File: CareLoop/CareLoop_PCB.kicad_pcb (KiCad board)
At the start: 2 copper layers, 67 parts, among them J1 Conn_Coaxial_Small, J1_Battery1 Conn_01x02_Pin, J1_DEBUG1 Conn_01x04_Pin, J2 USB_B_Micro, U1 MCP1700x-180xxMB, U2 MAX30102, U3 MPU-6050, U4 MCP1700x-330xxMB, U5 TP4056-42-ESOP8, U6 nRF52840-QFXX, U7 PCA9306, Y1 32MHz, Y2 32.768kHz

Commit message: update
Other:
- copper layers 2 -> 6
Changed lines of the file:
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@@
 	(layers
 		(0 "F.Cu" signal)
+		(4 "In1.Cu" signal)
+		(6 "In2.Cu" signal)
+		(8 "In3.Cu" signal)
+		(10 "In4.Cu" signal)
 		(2 "B.Cu" signal)
 		(9 "F.Adhes" user "F.Adhesive")
@@
 			)
 			(layer "dielectric 1"
-				(type "core")
-				(thickness 0.8)
+				(type "prepreg")
+				(thickness 0.1)
 				(material "FR4")
 				(epsilon_r 4.3)
 				(loss_tangent 0.02)
 			)
+			(layer "In1.Cu"
+				(type "copper")
+				(thickness 0.035)
+			)
+			(layer "dielectric 2"
+				(type "core")
+				(thickness 0.18)
+				(material "FR4")
+				(epsilon_r 4.5)
+				(loss_tangent 0.02)
+			)
+			(layer "In2.Cu"
+				(type "copper")
+				(thickness 0.035)
+			)
+			(layer "dielectric 3"
+				(type "prepreg")
+				(thickness 0.1)
+				(material "FR4")
+				(epsilon_r 4.5)
+				(loss_tangent 0.02)
+			)
+			(layer "In3.Cu"
+				(type "copper")
+				(thickness 0.035)
+			)
+			(layer "dielectric 4"
+				(type "core")
+				(thickness 0.18)
+				(material "FR4")
+				(epsilon_r 4.5)
+				(loss_tangent 0.02)
+			)
+			(layer "In4.Cu"
+				(type "copper")
+				(thickness 0.035)
+			)
+			(layer "dielectric 5"
+				(type "prepreg")
+				(thickness 0.1)
+				(material "FR4")
+				(epsilon_r 4.5)
+				(loss_tangent 0.02)
+			)

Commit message: update routing
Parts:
- added C13: 100n, Capacitor_SMD:C_0201_0603Metric_Pad0.64x0.40mm_HandSolder, F.Cu at (194.1, 87.2)
- added C13: 100n, Capacitor_SMD:C_0201_0603Metric_Pad0.64x0.40mm_HandSolder, F.Cu at (191.2, 85.7)
- added C13: 100n, Capacitor_SMD:C_0201_0603Metric_Pad0.64x0.40mm_HandSolder, F.Cu at (197.9, 78.0)
- added C13: 100n, Capacitor_SMD:C_0201_0603Metric_Pad0.64x0.40mm_HandSolder, F.Cu at (197.9, 87.0)
- added R5: 4k7, Resistor_SMD:R_0402_1005Metric_Pad0.72x0.64mm_HandSolder, F.Cu at (190.4, 82.5)
- C10, C11, C26, C27, C32, C40, C41, C7, C9, R21, R22, R23, R42, Y2: moved to B.Cu
- U5: footprint Package_SO:SOIC-8-1EP_3.9x4.9mm_P1.27mm_EP2.41x3.3mm_ThermalVias -> Package_SO:SOIC-8-1EP_3.9x4.9mm_P1.27mm_EP2.41x3.81mm; moved to B.Cu
- moved C43 60.9 mm to (205.2, 74.8), turned to 0 degrees
- moved C42 60.9 mm to (205.3, 71.7), turned to 0 degrees
- moved U4 53.2 mm to (201.7, 73.3)
- moved J1_Battery1 50.4 mm to (192.6, 92.8), turned to 180 degrees
- moved JP2_MPU1 49.3 mm to (193.2, 73.0)
- moved R42 38.9 mm to (182.8, 78.9), turned to 90 degrees
- moved JP2_MPU2 36.9 mm to (183.6, 82.6)
- moved C31 36.8 mm to (185.1, 81.1), turned to 90 degrees
- moved C21 36.4 mm to (178.9, 74.3)
- moved C20 36.3 mm to (177.7, 74.5)
- moved D3 36.1 mm to (193.7, 88.2)
- moved C30 36.0 mm to (183.3, 80.7), turned to 0 degrees
- moved C32 35.4 mm to (186.2, 81.5), turned to -90 degrees
- moved C23 34.9 mm to (192.4, 82.3)
- moved R4 34.8 mm to (195.7, 87.7), turned to -90 degrees
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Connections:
- net Net-(U1-VO) renamed /MAX30102/VCC_1.8V
- AE1 pad 2: GND -> unconnected-(AE1-PCB_Trace-Pad2)
- R20 pad 1: Net-(JP1_MAX30102-A) -> /Battery/VCC
- R4 pad 1: Net-(U6-P0.07) -> /MCU/Status_LED
- U6 pad 13: /MAX30102/MAX_INT -> unconnected-(U6-P0.13-Pad13)
- U6 pad 19: unconnected-(U6-P0.20-Pad19) -> /MCU/Status_LED
- U6 pad 22: unconnected-(U6-P0.23-Pad22) -> /MAX30102/MAX_INT
- U6 pad 6: Net-(U6-P0.07) -> unconnected-(U6-P0.07-Pad6)
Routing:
- net /Battery/VCC: track 85.3 -> 20.7 mm, vias 4 -> 17
- net Net-(J1_Battery1-Pin_2): track 21.3 -> 48.2 mm, vias 0 -> 1
- net /MAX30102/VCC_1.8V: track 29.0 -> 4.55 mm, vias 1 -> 5
- net GND: track 11.6 -> 29.2 mm, vias 3 -> 68
- net /MCU/INT_MPU: track 25.2 -> 8.68 mm
- net Net-(JP1_MAX30102-A): track 53.6 -> 38.4 mm, vias 1 -> 2
- net /MAX30102/MAX_INT: track 26.1 -> 10.9 mm
- net Net-(U6-DEC4): track 29.2 -> 14.3 mm, vias 0 -> 2
- net /MAX30102/SDA: track 34.4 -> 25.4 mm
- net Net-(D41-K): track 8.70 -> 0.00 mm, vias 0 -> 1
- net Net-(U6-~{RESET}): track 9.00 -> 17.0 mm
- net Net-(U2-SCL): track 19.5 -> 11.6 mm
- net Net-(J2-VBUS): track 12.6 -> 20.0 mm, vias 0 -> 2
- net /Antenna/ANT: track 7.09 -> 1.58 mm
- net Net-(U7-EN): track 8.19 -> 3.85 mm, vias 0 -> 1
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- added copper zone on In2.Cu, net /Battery/VCC
- added copper zone on In3.Cu, net /MAX30102/VCC_1.8V
- added copper zone on In1.Cu, net GND
- added copper zone on In4.Cu, net GND
- removed copper zone on B.Cu, net GND
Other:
- board outline added: 40.5 x 24 mm
- board text added: "CareLoop_Prototype_V1"

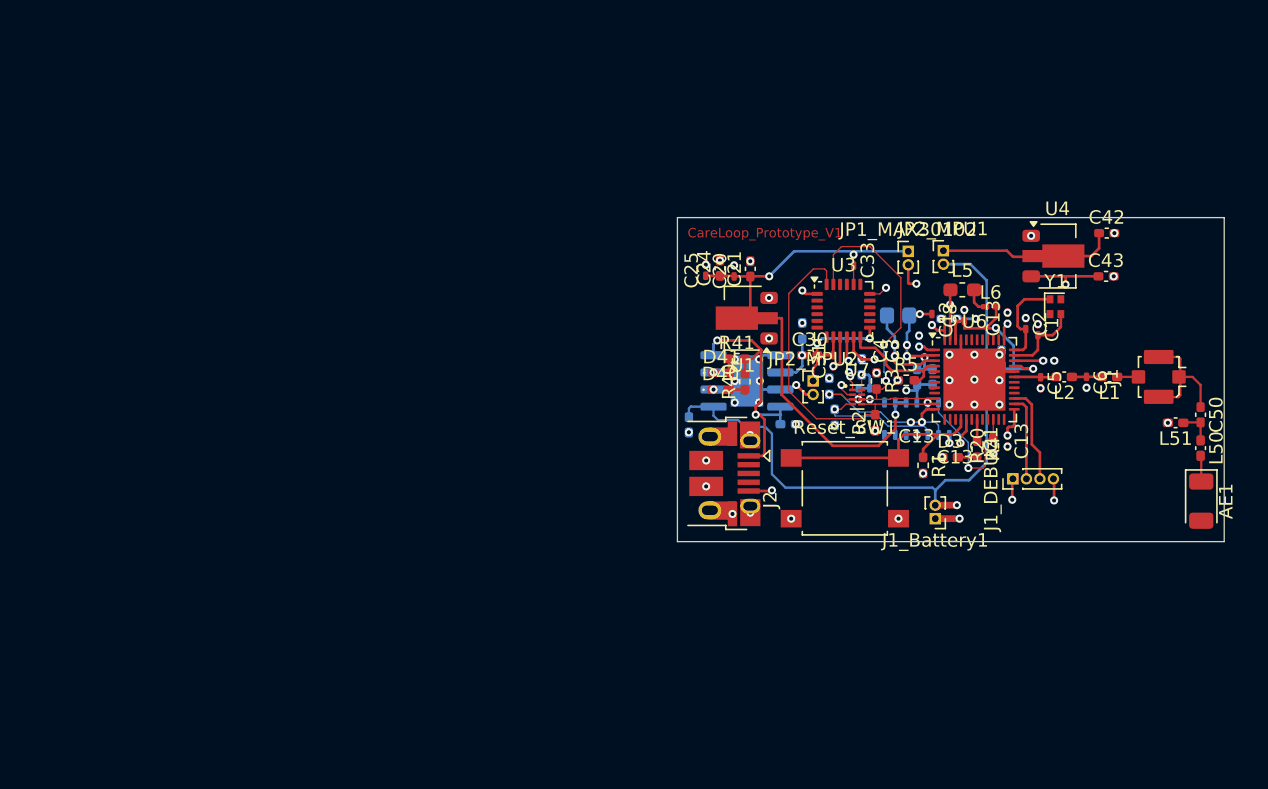
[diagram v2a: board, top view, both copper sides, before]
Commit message: updated vias
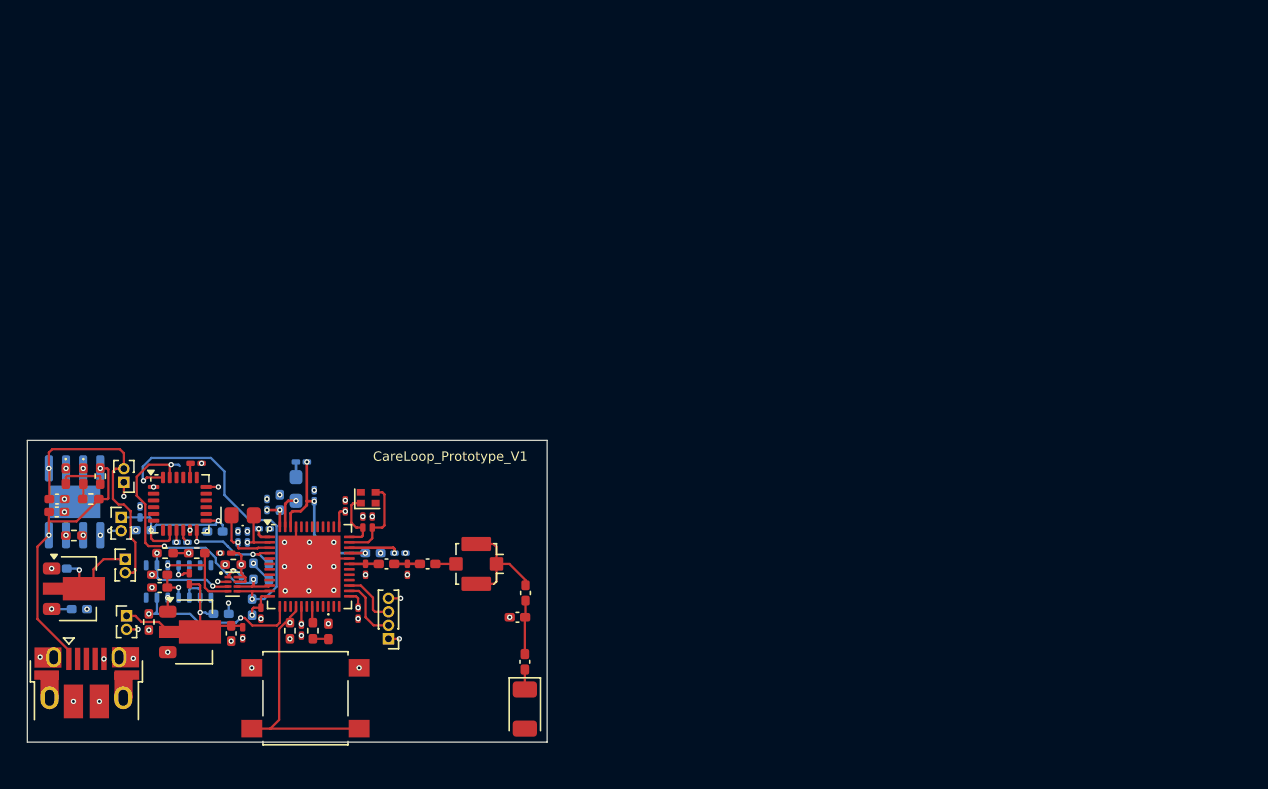
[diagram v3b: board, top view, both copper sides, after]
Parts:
- removed the C10 at (191.4, 79.7)
- removed C13 (x4): 100n, Capacitor_SMD:C_0201_0603Metric_Pad0.64x0.40mm_HandSolder
- removed the C30 at (183.3, 80.7)
- added C10: 100p, Capacitor_SMD:C_0201_0603Metric_Pad0.64x0.40mm_HandSolder, F.Cu at (142.7, 99.8)
- added C10: 100p, Capacitor_SMD:C_0201_0603Metric_Pad0.64x0.40mm_HandSolder, F.Cu at (148.9, 91.8)
- added C10: 100p, Capacitor_SMD:C_0201_0603Metric_Pad0.64x0.40mm_HandSolder, F.Cu at (145.7, 101.0)
- added C10: 100p, Capacitor_SMD:C_0201_0603Metric_Pad0.64x0.40mm_HandSolder, F.Cu at (149.8, 99.8)
- added C10: 100p, Capacitor_SMD:C_0201_0603Metric_Pad0.64x0.40mm_HandSolder, B.Cu at (142.9, 93.5)
- added C30: 10n, Capacitor_SMD:C_0402_1005Metric_Pad0.74x0.62mm_HandSolder, B.Cu at (139.2, 93.8)
- added C30: 10n, Capacitor_SMD:C_0402_1005Metric_Pad0.74x0.62mm_HandSolder, B.Cu at (133.9, 93.7)
- C12, C24, C3, C31, C4, C42, C43, C8, L5, L6, R2, R3, R5: moved to B.Cu
- C22, C23, C26, C40, C41, R21, R22, R23, R42, Y2: moved to F.Cu
- moved C42 81.5 mm to (127.7, 96.5), turned to 180 degrees
- moved C43 79.9 mm to (129.2, 99.5)
- moved U4 76.6 mm to (129.1, 98.0)
- moved JP2_MPU1 64.8 mm to (132.6, 95.8)
- moved R20 63.9 mm to (134.3, 100.5)
- moved JP1_MAX30102 63.9 mm to (132.7, 100.0)
- moved J1_Battery1 60.2 mm to (132.5, 90.1)
- moved C23 59.1 mm to (135.2, 97.0), turned to 180 degrees
- moved C22 58.2 mm to (135.2, 97.9), turned to 180 degrees
- moved R42 56.0 mm to (128.8, 94.0), turned to 180 degrees
- moved U2 56.0 mm to (136.6, 97.5), turned to -90 degrees
- moved C40 54.6 mm to (127.5, 92.3)
- moved Y1 52.8 mm to (150.6, 91.2), turned to 90 degrees
- moved C31 52.6 mm to (133.7, 92.3), turned to -90 degrees
- moved L50 52.5 mm to (162.2, 103.4)
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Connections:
- net Net-(D40-K) renamed /Battery/STDBY
- net Net-(D41-K) renamed /Battery/CHRG
- net Net-(J1_Battery1-Pin_2) renamed /Battery/BAT_Plus
- net Net-(J1_DEBUG1-Pin_2) renamed /MCU/SWDIO
- net Net-(J1_DEBUG1-Pin_3) renamed /MCU/SWDCLK
- net Net-(J2-VBUS) renamed /Battery/VBUS
- net Net-(JP1_MAX30102-A) renamed /MAX30102/VIN_MAX30102
- net Net-(JP2_MPU1-A) renamed /Battery/VIN_BATTERY
- net Net-(JP2_MPU2-A) renamed /MPU6050/VIN_MPU
- net Net-(U2-SCL) renamed /MAX30102/SCL1
- net Net-(U2-SDA) renamed /MAX30102/SDA1
- net Net-(U3-CPOUT) renamed /MPU6050/CPOUT
- net Net-(U3-REGOUT) renamed /MPU6050/REGOUT
- net Net-(U5-PROG) renamed /Battery/PROG
- net Net-(U6-ANT) renamed /MCU/ANT_PIN
- net Net-(U6-DCC) renamed /MCU/DCC
- net Net-(U6-DEC3) renamed /MCU/DEC3
- net Net-(U6-DEC4) renamed /MCU/DEC4/DEC6
- net Net-(U6-~{RESET}) renamed /MCU/Reset
- U6 pad 1: Net-(U6-DEC1) -> /MCU/DEC1
- U6 pad 13: unconnected-(U6-P0.13-Pad13) -> /MAX30102/MAX_INT
- U6 pad 22: /MAX30102/MAX_INT -> unconnected-(U6-P0.23-Pad22)
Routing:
- net /Battery/BAT_Plus: track 48.2 -> 20.4 mm
- net /MAX30102/VIN_MAX30102: track 38.4 -> 13.7 mm, vias 2 -> 1
- net GND: track 29.2 -> 10.3 mm, vias 68 -> 59
- net /Battery/VCC: track 20.7 -> 14.7 mm, vias 17 -> 14
- net /MAX30102/SCL1: track 11.6 -> 7.37 mm, vias 1 -> 2
- net /Battery/VIN_BATTERY: track 9.48 -> 5.48 mm, vias 0 -> 1
- net /Battery/PROG: track 3.82 -> 0.00 mm, vias 0 -> 1
- net /MCU/SWDCLK: track 7.23 -> 4.23 mm
- net /MPU6050/VIN_MPU: track 10.3 -> 13.1 mm
- net /MAX30102/SDA1: track 9.64 -> 7.13 mm
- net Net-(D40-A): track 1.23 -> 3.64 mm
- net Net-(U6-XC2): track 7.07 -> 4.69 mm
- net /MAX30102/MAX_INT: track 10.9 -> 12.9 mm, vias 1 -> 2
- net /MAX30102/SCL: track 24.0 -> 22.3 mm, vias 2 -> 3
- net Net-(U6-P0.01): track 6.83 -> 5.19 mm
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- added copper zone on In4.Cu, net /MAX30102/VCC_1.8V
- added copper zone on In3.Cu, net GND
- removed copper zone on In3.Cu, net /MAX30102/VCC_1.8V
- removed copper zone on In4.Cu, net GND
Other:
- board size 40.5 x 24 mm -> 38.5 x 22.3 mm

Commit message: updated version
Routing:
- net GND: vias 59 -> 87
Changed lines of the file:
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@@
+	)
+	(gr_rect
+		(start 157.05 102.5)
+		(end 163.85 109.35)
+		(stroke
+			(width 0.1)
+			(type default)
+		)
+		(fill no)
+		(layer "B.Paste")
 	)
 	(gr_rect
@@
 	)
 	(via
+		(at 155 97.25)
+		(size 0.4)
+		(drill 0.2)
+		(layers "F.Cu" "B.Cu")
+		(free yes)
+		(net 2)
+	)
+	(via
 		(at 130.685 106.335)
 		(size 0.4)
@@
 	)
 	(via
+		(at 163.2 102.5)
+		(size 0.4)
+		(drill 0.2)
+		(layers "F.Cu" "B.Cu")
+		(free yes)
+		(net 2)
+	)
+	(via
+		(at 162.1 96.4)
+		(size 0.4)
+		(drill 0.2)
+		(layers "F.Cu" "B.Cu")
+		(free yes)
+		(net 2)
+	)
+	(via
+		(at 161 96.95)
+		(size 0.4)
+		(drill 0.2)
+		(layers "F.Cu" "B.Cu")
+		(free yes)
+		(net 2)
+	)
+	(via
 		(at 146.25 94.55)
 		(size 0.4)
@@
 	)
 	(via
+		(at 163 100.5)
+		(size 0.4)
+		(drill 0.2)
+		(layers "F.Cu" "B.Cu")
+		(free yes)
+		(net 2)
+	)
+	(via
 		(at 148.05 96.35)
 		(size 0.4)
@@
 	)
 	(via
+		(at 160 102.5)
+		(size 0.4)
+		(drill 0.2)
+		(layers "F.Cu" "B.Cu")
+		(free yes)
+		(net 2)
+	)
+	(via
 		(at 135.75 98.65)
 		(size 0.4)
@@
 	)
 	(via
+		(at 163 101.65)
+		(size 0.4)
+		(drill 0.2)
+		(layers "F.Cu" "B.Cu")
+		(free yes)
+		(net 2)
+	)
+	(via
+		(at 163 99.45)
+		(size 0.4)
+		(drill 0.2)
+		(layers "F.Cu" "B.Cu")
+		(free yes)
+		(net 2)
+	)
+	(via
 		(at 126.3 103.05)
 		(size 0.4)
@@
 	)
 	(via
+		(at 157.05 107.5)
+		(size 0.4)
+		(drill 0.2)
+		(layers "F.Cu" "B.Cu")
+		(free yes)
+		(net 2)
+	)
+	(via
 		(at 143.1 91.3425)
 		(size 0.4)
@@
 	)
 	(via
+		(at 157.05 108.5)
+		(size 0.4)
+		(drill 0.2)
+		(layers "F.Cu" "B.Cu")
+		(free yes)
+		(net 2)
+	)
+	(via
 		(at 128.1 92.3)
 		(size 0.4)
@@
 	)
 	(via
+		(at 159 102.5)
+		(size 0.4)
+		(drill 0.2)
+		(layers "F.Cu" "B.Cu")
+		(free yes)
+		(net 2)
+	)
+	(via
 		(at 140.6 96.65)
 		(size 0.4)
@@
 	)
 	(via
+		(at 157.05 102.55)
+		(size 0.4)
+		(drill 0.2)
+		(layers "F.Cu" "B.Cu")
+		(free yes)
+		(net 2)
+	)
+	(via
 		(at 132.5 91.15)
 		(size 0.4)
@@
 	)
 	(via
+		(at 155 95.25)
+		(size 0.4)
+		(drill 0.2)
+		(layers "F.Cu" "B.Cu")
+		(free yes)
+		(net 2)
+	)
+	(via
 		(at 141.3 101.6575)
 		(size 0.4)
@@
 	)
 	(via
+		(at 158 102.5)
+		(size 0.4)
+		(drill 0.2)
+		(layers "F.Cu" "B.Cu")
+		(free yes)
+		(net 2)
+	)
+	(via
 		(at 144.05 91.0325)
 		(size 0.4)
@@
 	)
 	(via
+		(at 161.1 102.5)
+		(size 0.4)
+		(drill 0.2)
+		(layers "F.Cu" "B.Cu")
+		(free yes)
+		(net 2)
+	)
+	(via
 		(at 147.65 100.5775)
 		(size 0.4)
@@
 	)
 	(via
+		(at 161.5 101.65)
+		(size 0.4)
+		(drill 0.2)
+		(layers "F.Cu" "B.Cu")
+		(free yes)
+		(net 2)
+	)
+	(via
 		(at 144.45 98.15)
 		(size 0.4)
@@
 	)
 	(via
+		(at 163 98.45)
+		(size 0.4)
+		(drill 0.2)
+		(layers "F.Cu" "B.Cu")
+		(free yes)
+		(net 2)
+	)
+	(via
 		(at 141.975 103.85)
 		(size 0.4)
@@
 	)
 	(via
+		(at 156.25 95.25)
+		(size 0.4)
+		(drill 0.2)
+		(layers "F.Cu" "B.Cu")
+		(free yes)
+		(net 2)
+	)
+	(via
 		(at 146.25 96.35)
 		(size 0.4)
@@
 	)
 	(via
+		(at 163 97.45)
+		(size 0.4)
+		(drill 0.2)
+		(layers "F.Cu" "B.Cu")
+		(free yes)
+		(net 2)
+	)
+	(via
 		(at 151.5175 95.35)
 		(size 0.4)
@@
 	)
 	(via
+		(at 157.05 103.5)
+		(size 0.4)
+		(drill 0.2)
+		(layers "F.Cu" "B.Cu")
+		(free yes)
+		(net 2)
+	)
+	(via
+		(at 161.5 97.45)
+		(size 0.4)
+		(drill 0.2)
+		(layers "F.Cu" "B.Cu")
+		(free yes)
+		(net 2)
+	)
+	(via
+		(at 157.05 104.5)
+		(size 0.4)
+		(drill 0.2)
+		(layers "F.Cu" "B.Cu")
+		(free yes)
+		(net 2)
+	)
+	(via
 		(at 128.765 106.335)
 		(size 0.4)
@@
 	)
 	(via
+		(at 157.05 106.5)
+		(size 0.4)
+		(drill 0.2)
+		(layers "F.Cu" "B.Cu")
+		(free yes)
+		(net 2)
+	)
+	(via
 		(at 143.3075 93.55)
 		(size 0.4)
@@
 	)
 	(via
+		(at 157.05 105.5)
+		(size 0.4)
+		(drill 0.2)
+		(layers "F.Cu" "B.Cu")
+		(free yes)
+		(net 2)
+	)
+	(via
 		(at 150.9 92.6425)
 		(size 0.4)
@@
 	)
 	(via
+		(at 161 95.5)
+		(size 0.4)
+		(drill 0.2)
+		(layers "F.Cu" "B.Cu")
+		(free yes)
+		(net 2)
+	)
+	(via
 		(at 150.2 92.6425)
 		(size 0.4)
@@
 		(net 2)
 	)
+	(via
+		(at 156.25 97.25)
+		(size 0.4)
+		(drill 0.2)
+		(layers "F.Cu" "B.Cu")
+		(free yes)
+		(net 2)
+	)
+	(via
+		(at 161.5 98.45)
+		(size 0.4)
+		(drill 0.2)
+		(layers "F.Cu" "B.Cu")
+		(free yes)
+		(net 2)
+	)
+	(via
+		(at 161.5 99.45)
+		(size 0.4)
+		(drill 0.2)
+		(layers "F.Cu" "B.Cu")
+		(free yes)
+		(net 2)
+	)

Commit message: PCB V1.0
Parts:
- C13, C14, C15, C16: renamed from C10; value 100p -> 100n
- moved J1 0.20 mm to (158.4, 96.1)
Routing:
- net /Battery/VIN_BATTERY: track 5.48 -> 6.76 mm
- net /MAX30102/SCL: track 22.3 -> 21.5 mm
- net /Battery/VCC: track 14.7 -> 15.3 mm
- added copper zone on B.Cu, net GND
- added copper zone on F.Cu, net GND

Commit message: PCB update
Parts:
- moved J1 0.20 mm to (158.6, 96.2)
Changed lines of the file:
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@@
 	(footprint "Connector_Coaxial:U.FL_Molex_MCRF_73412-0110_Vertical"
 		(layer "F.Cu")
-		(at 158.4 96.125 -90)
+		(at 158.6 96.15 -90)
 		(descr "Molex Microcoaxial RF Connectors (MCRF), mates Hirose U.FL, (http://www.molex.com/pdm_docs/sd/734120110_sd.pdf)")
 		(tags "mcrf hirose ufl u.fl microcoaxial")
@@
 	)
 	(segment
-		(start 139.8175 93.2675)
-		(end 139.5 92.95)
-		(width 0.17)
-		(layer "B.Cu")
-		(net 77)
-	)
-	(segment
 		(start 139.8175 93.75)
 		(end 139.8175 93.2675)
@@
 	)
 	(segment
+		(start 139.75 92.95)
+		(end 139.5 92.95)
+		(width 0.17)
+		(layer "B.Cu")
+		(net 77)
+	)
+	(segment
 		(start 134.5175 92.8175)
 		(end 134.5175 93.65)
@@
 		(width 0.17)
 		(layer "B.Cu")
+		(net 77)
+	)
+	(segment
+		(start 139.8175 93.2675)
+		(end 139.8175 93.0175)
+		(width 0.17)
+		(layer "B.Cu")
+		(net 77)
+	)
+	(segment
+		(start 139.8175 93.0175)
+		(end 139.75 92.95)
+		(width 0.17)
+		(layer "B.Cu")
